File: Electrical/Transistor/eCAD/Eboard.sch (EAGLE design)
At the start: 22 parts

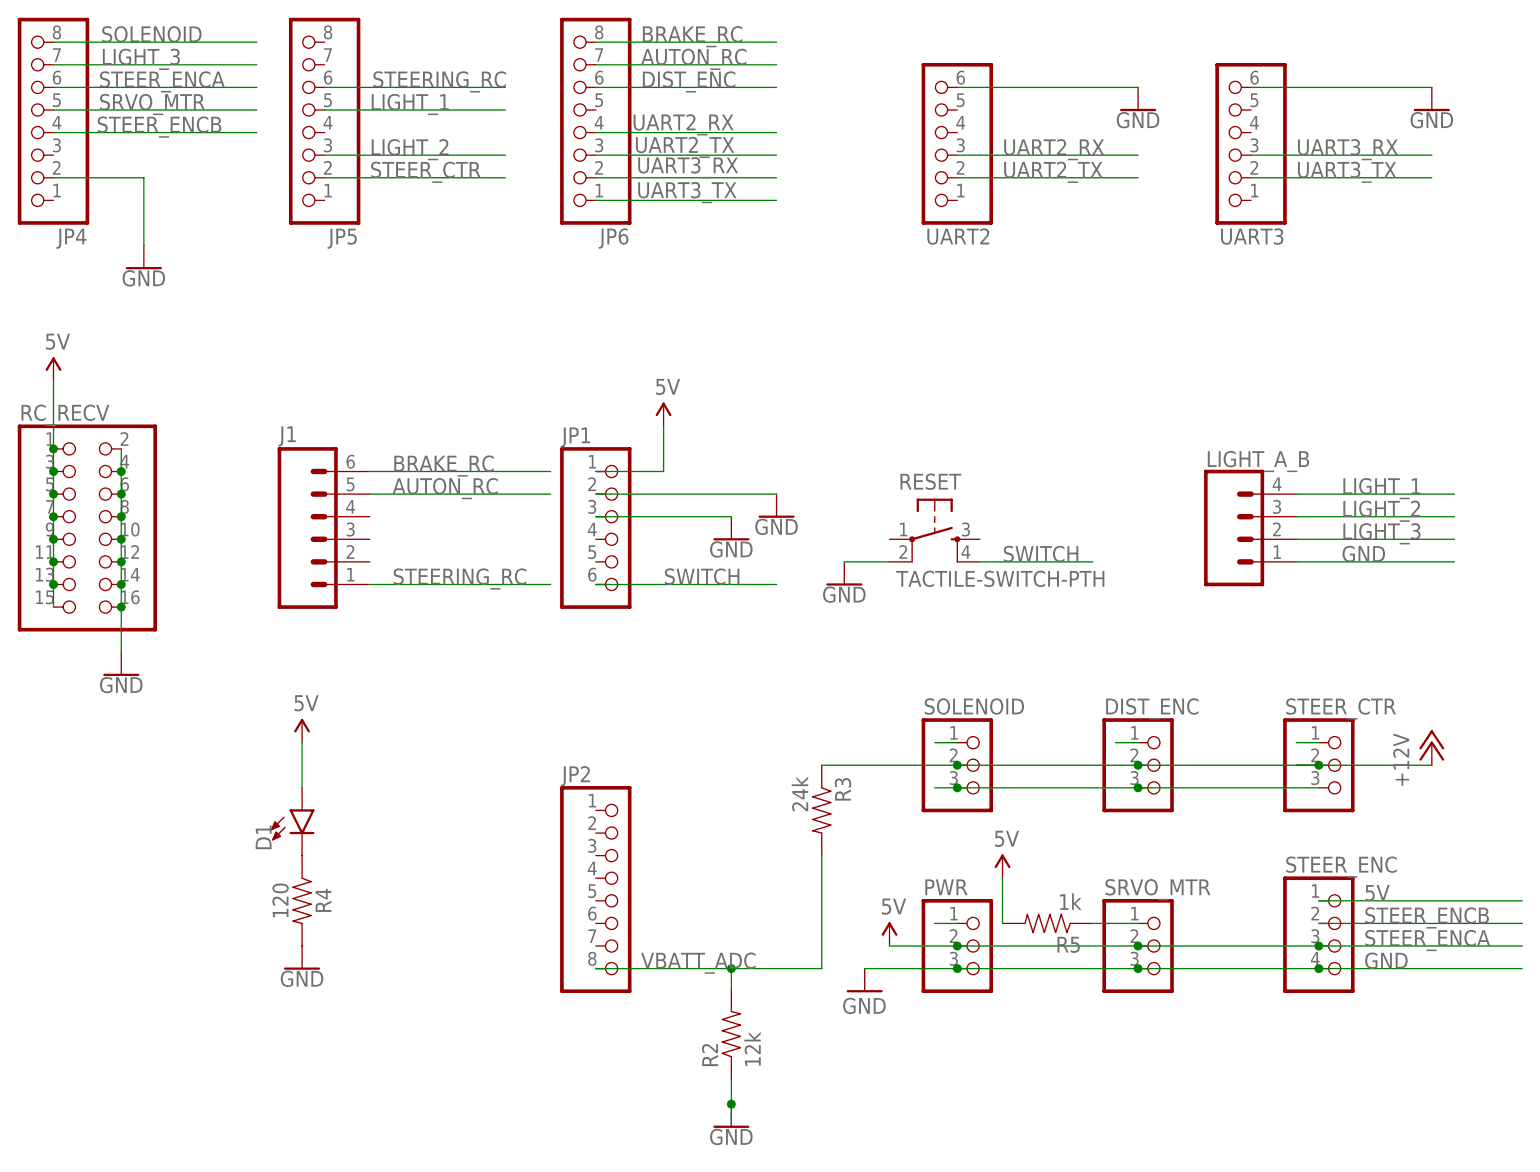
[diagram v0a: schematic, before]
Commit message: checked to see if trace connections in schematic were sensical, added ground and 5V symbols to schematic for readability, checked alignment of pin sets in board file for alignment, rerouted board file based on amendments in schematic, checked that 12V traces were 40 mils, 5V traces were 16 mils, and all other traces (incl. VBATT_ADC) were 10 mils
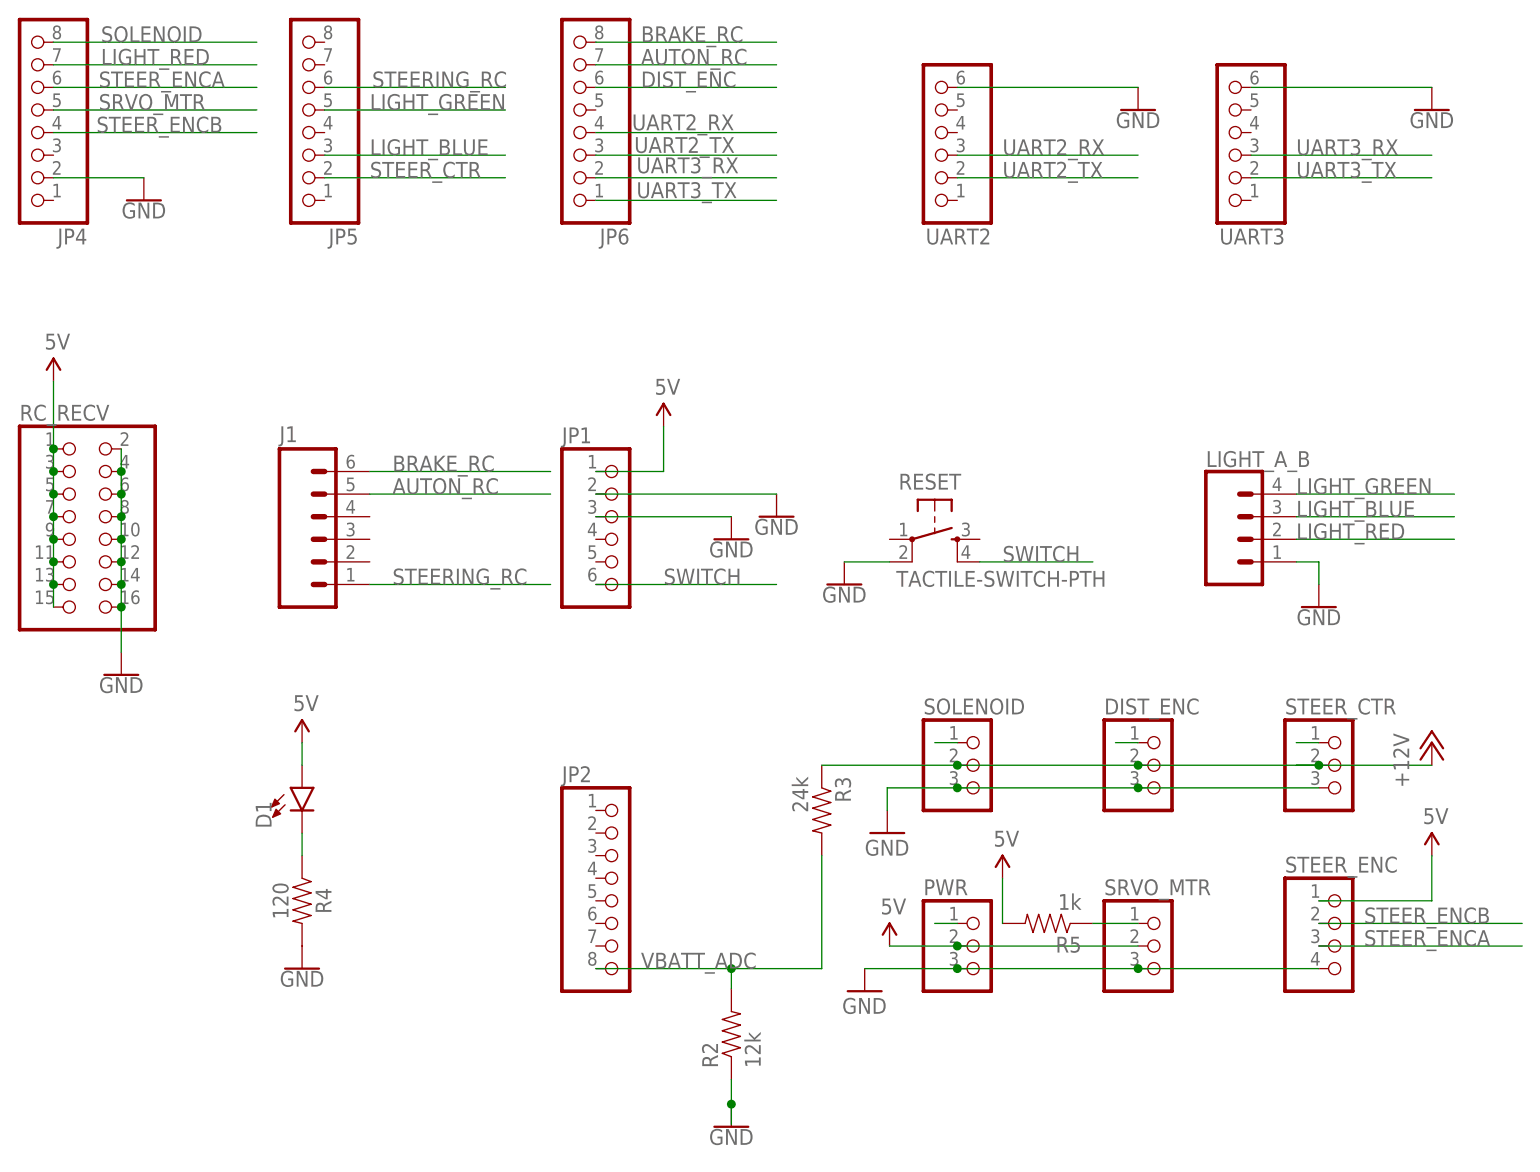
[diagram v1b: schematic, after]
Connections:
- net LIGHT_1 renamed LIGHT_GREEN
- net LIGHT_2 renamed LIGHT_BLUE
- net LIGHT_3 renamed LIGHT_RED
- net 5V: now also PWR.2, SRVO_MTR.2
- net STEER_ENCA: no longer PWR.2, SRVO_MTR.2
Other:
- moved on the sheet: D1
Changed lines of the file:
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@@
 </classes>
 <parts>
-<part name="GND2" library="supply1" deviceset="GND" device=""/>
+<part name="GND" library="supply1" deviceset="GND" device=""/>
 <part name="FRAME1" library="frames" deviceset="LETTER_L" device=""/>
 <part name="SOLENOID" library="pinhead" deviceset="PINHD-1X3" device=""/>
@@
 <part name="SUPPLY5" library="SparkFun-Aesthetics" deviceset="5V" device=""/>
 <part name="GND10" library="SparkFun-PowerSymbols" library_urn="urn:adsk.eagle:library:530" deviceset="GND" device=""/>
+<part name="GND2" library="SparkFun-PowerSymbols" library_urn="urn:adsk.eagle:library:530" deviceset="GND" device=""/>
+<part name="GND11" library="supply1" deviceset="GND" device=""/>
+<part name="SUPPLY6" library="SparkFun-Aesthetics" deviceset="5V" device=""/>
 </parts>
 <sheets>
@@
 </plain>
 <instances>
-<instance part="GND2" gate="1" x="149.606" y="71.12"/>
+<instance part="GND" gate="1" x="149.606" y="71.12"/>
 <instance part="FRAME1" gate="G$1" x="0" y="0"/>
 <instance part="FRAME1" gate="G$2" x="147.32" y="0"/>
@@
 <instance part="JP6" gate="A" x="116.84" y="170.18" rot="R180"/>
 <instance part="STEER_ENC" gate="A" x="203.2" y="76.2"/>
-<instance part="D1" gate="G$1" x="86.36" y="91.44"/>
+<instance part="D1" gate="G$1" x="86.36" y="93.98"/>
 <instance part="LIGHT_A_B" gate="G$1" x="193.04" y="121.92"/>
 <instance part="R4" gate="G$1" x="86.36" y="81.28" rot="R270"/>
@@
 <instance part="SUPPLY4" gate="G$1" x="58.42" y="139.7"/>
 <instance part="SUPPLY5" gate="G$1" x="127" y="134.62"/>
-<instance part="GND10" gate="1" x="68.58" y="152.4"/>
+<instance part="GND10" gate="1" x="68.58" y="160.02"/>
+<instance part="GND2" gate="1" x="200.66" y="114.3"/>
+<instance part="GND11" gate="1" x="152.146" y="88.9"/>
+<instance part="SUPPLY6" gate="G$1" x="213.36" y="86.36"/>
 </instances>
 <busses>
@@
 <pinref part="D1" gate="G$1" pin="A"/>
 <pinref part="SUPPLY3" gate="G$1" pin="5V"/>
-<wire x1="86.36" y1="93.98" x2="86.36" y2="99.06" width="0.1524" layer="91"/>
+<wire x1="86.36" y1="96.52" x2="86.36" y2="99.06" width="0.1524" layer="91"/>
 </segment>
 <segment>
@@
 </segment>
 <segment>
+<pinref part="PWR" gate="A" pin="2"/>
+<pinref part="SRVO_MTR" gate="A" pin="2"/>
+<wire x1="160.02" y1="76.2" x2="180.34" y2="76.2" width="0.1524" layer="91"/>
+<pinref part="SUPPLY1" gate="G$1" pin="5V"/>
+<wire x1="152.4" y1="76.2" x2="160.02" y2="76.2" width="0.1524" layer="91"/>
+<junction x="160.02" y="76.2"/>
+</segment>
+<segment>
 <pinref part="STEER_ENC" gate="A" pin="1"/>
-<label x="205.74" y="81.28" size="1.778" layer="95"/>
-<wire x1="200.66" y1="81.28" x2="223.52" y2="81.28" width="0.1524" layer="91"/>
+<wire x1="200.66" y1="81.28" x2="213.36" y2="81.28" width="0.1524" layer="91"/>
+<wire x1="213.36" y1="81.28" x2="213.36" y2="86.36" width="0.1524" layer="91"/>
+<pinref part="SUPPLY6" gate="G$1" pin="5V"/>
 </segment>
 </net>
@@
 </segment>
 <segment>
-<pinref part="GND2" gate="1" pin="GND"/>
-<wire x1="149.606" y1="73.66" x2="154.94" y2="73.66" width="0.1524" layer="91"/>
+<pinref part="GND" gate="1" pin="GND"/>
+<wire x1="149.606" y1="73.66" x2="160.02" y2="73.66" width="0.1524" layer="91"/>
 <pinref part="PWR" gate="A" pin="3"/>
-<wire x1="154.94" y1="73.66" x2="155.702" y2="73.66" width="0.1524" layer="91"/>
-<wire x1="160.02" y1="73.66" x2="155.702" y2="73.66" width="0.1524" layer="91"/>
 <pinref part="SRVO_MTR" gate="A" pin="3"/>
 <wire x1="160.02" y1="73.66" x2="180.34" y2="73.66" width="0.1524" layer="91"/>
@@
 <junction x="180.34" y="73.66"/>
 <pinref part="STEER_ENC" gate="A" pin="4"/>
-<label x="205.74" y="73.66" size="1.778" layer="95"/>
-<wire x1="200.66" y1="73.66" x2="223.52" y2="73.66" width="0.1524" layer="91"/>
-<junction x="200.66" y="73.66"/>
 <wire x1="180.34" y1="73.66" x2="200.66" y2="73.66" width="0.1524" layer="91"/>
 </segment>
@@
 <segment>
 <pinref part="SOLENOID" gate="A" pin="3"/>
-<wire x1="160.02" y1="93.98" x2="157.48" y2="93.98" width="0.1524" layer="91"/>
-<junction x="160.02" y="93.98"/>
 <pinref part="DIST_ENC" gate="A" pin="3"/>
 <junction x="180.34" y="93.98"/>
@@
 <wire x1="180.34" y1="93.98" x2="200.66" y2="93.98" width="0.1524" layer="91"/>
 <wire x1="160.02" y1="93.98" x2="180.34" y2="93.98" width="0.1524" layer="91"/>
-</segment>
-<segment>
-<pinref part="LIGHT_A_B" gate="G$1" pin="1"/>
-<label x="203.2" y="119.38" size="1.778" layer="95"/>
-<wire x1="198.12" y1="119.38" x2="215.9" y2="119.38" width="0.1524" layer="91"/>
+<pinref part="GND11" gate="1" pin="GND"/>
+<wire x1="160.02" y1="93.98" x2="152.146" y2="93.98" width="0.1524" layer="91"/>
+<wire x1="152.146" y1="93.98" x2="152.146" y2="91.44" width="0.1524" layer="91"/>
+<junction x="160.02" y="93.98"/>
 </segment>
 <segment>
@@
 <pinref part="JP4" gate="A" pin="2"/>
 <wire x1="58.42" y1="162.56" x2="68.58" y2="162.56" width="0.1524" layer="91"/>
-<wire x1="68.58" y1="162.56" x2="68.58" y2="154.94" width="0.1524" layer="91"/>
 <pinref part="GND10" gate="1" pin="GND"/>
 </segment>
@@
 <pinref part="R4" gate="G$1" pin="2"/>
 <pinref part="GND4" gate="1" pin="GND"/>
+</segment>
+<segment>
+<pinref part="LIGHT_A_B" gate="G$1" pin="1"/>
+<pinref part="GND2" gate="1" pin="GND"/>
+<wire x1="198.12" y1="119.38" x2="200.66" y2="119.38" width="0.1524" layer="91"/>
+<wire x1="200.66" y1="119.38" x2="200.66" y2="116.84" width="0.1524" layer="91"/>
 </segment>
 </net>
@@
 </segment>
 <segment>
-<pinref part="PWR" gate="A" pin="2"/>
-<pinref part="SRVO_MTR" gate="A" pin="2"/>
-<wire x1="160.02" y1="76.2" x2="180.34" y2="76.2" width="0.1524" layer="91"/>
-<junction x="180.34" y="76.2"/>
 <pinref part="STEER_ENC" gate="A" pin="3"/>
+<wire x1="200.66" y1="76.2" x2="223.52" y2="76.2" width="0.1524" layer="91"/>
 <label x="205.74" y="76.2" size="1.778" layer="95"/>
-<wire x1="200.66" y1="76.2" x2="223.52" y2="76.2" width="0.1524" layer="91"/>
-<junction x="200.66" y="76.2"/>
-<wire x1="180.34" y1="76.2" x2="200.66" y2="76.2" width="0.1524" layer="91"/>
-<pinref part="SUPPLY1" gate="G$1" pin="5V"/>
-<wire x1="152.4" y1="76.2" x2="160.02" y2="76.2" width="0.1524" layer="91"/>
-<junction x="160.02" y="76.2"/>
 </segment>
 </net>
@@
 </segment>
 </net>
-<net name="LIGHT_1" class="0">
+<net name="LIGHT_GREEN" class="0">
 <segment>
 <pinref part="LIGHT_A_B" gate="G$1" pin="4"/>
-<label x="203.2" y="127" size="1.778" layer="95"/>
+<label x="198.12" y="127" size="1.778" layer="95"/>
 <wire x1="198.12" y1="127" x2="215.9" y2="127" width="0.1524" layer="91"/>
 </segment>
@@
 </segment>
 </net>
-<net name="LIGHT_2" class="0">
+<net name="LIGHT_BLUE" class="0">
 <segment>
 <pinref part="LIGHT_A_B" gate="G$1" pin="3"/>
-<label x="203.2" y="124.46" size="1.778" layer="95"/>
+<label x="198.12" y="124.46" size="1.778" layer="95"/>
 <wire x1="198.12" y1="124.46" x2="215.9" y2="124.46" width="0.1524" layer="91"/>
 </segment>
@@
 </segment>
 </net>
-<net name="LIGHT_3" class="0">
+<net name="LIGHT_RED" class="0">
 <segment>
 <pinref part="LIGHT_A_B" gate="G$1" pin="2"/>
-<label x="203.2" y="121.92" size="1.778" layer="95"/>
+<label x="198.12" y="121.92" size="1.778" layer="95"/>
 <wire x1="198.12" y1="121.92" x2="215.9" y2="121.92" width="0.1524" layer="91"/>
 </segment>
@@
 <pinref part="D1" gate="G$1" pin="C"/>
 <pinref part="R4" gate="G$1" pin="1"/>
-</segment>
-</net>
+<wire x1="86.36" y1="88.9" x2="86.36" y2="86.36" width="0.1524" layer="91"/>
+</segment>
+</net>

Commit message: updated the light names, updated the offset on shield to match arduino mega to resolve alignment issues in 1.7, updated silkscreen with labels for pins, added dimensions to tDocu layer in inches, double checked pins match on shield, checked that orientations for all pins were correct on board
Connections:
- net 5V: no longer JP1.1
- net LIGHT_BLUE: now also JP5.5, LIGHT_A_B.4; no longer JP5.3, LIGHT_A_B.3
- net LIGHT_GREEN: now also JP5.3, LIGHT_A_B.3; no longer JP5.5, LIGHT_A_B.4
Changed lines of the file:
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@@
 <part name="SUPPLY3" library="SparkFun-Aesthetics" deviceset="5V" device=""/>
 <part name="SUPPLY4" library="SparkFun-Aesthetics" deviceset="5V" device=""/>
-<part name="SUPPLY5" library="SparkFun-Aesthetics" deviceset="5V" device=""/>
 <part name="GND10" library="SparkFun-PowerSymbols" library_urn="urn:adsk.eagle:library:530" deviceset="GND" device=""/>
 <part name="GND2" library="SparkFun-PowerSymbols" library_urn="urn:adsk.eagle:library:530" deviceset="GND" device=""/>
@@
 <instance part="SUPPLY3" gate="G$1" x="86.36" y="99.06"/>
 <instance part="SUPPLY4" gate="G$1" x="58.42" y="139.7"/>
-<instance part="SUPPLY5" gate="G$1" x="127" y="134.62"/>
 <instance part="GND10" gate="1" x="68.58" y="160.02"/>
 <instance part="GND2" gate="1" x="200.66" y="114.3"/>
@@
 </segment>
 <segment>
-<pinref part="JP1" gate="A" pin="1"/>
-<wire x1="119.38" y1="129.54" x2="127" y2="129.54" width="0.1524" layer="91"/>
-<wire x1="127" y1="129.54" x2="127" y2="134.62" width="0.1524" layer="91"/>
-<pinref part="SUPPLY5" gate="G$1" pin="5V"/>
-</segment>
-<segment>
 <pinref part="PWR" gate="A" pin="2"/>
 <pinref part="SRVO_MTR" gate="A" pin="2"/>
@@
 <net name="LIGHT_GREEN" class="0">
 <segment>
+<pinref part="JP5" gate="A" pin="3"/>
+<label x="93.98" y="165.1" size="1.778" layer="95"/>
+<wire x1="88.9" y1="165.1" x2="109.22" y2="165.1" width="0.1524" layer="91"/>
+</segment>
+<segment>
+<pinref part="LIGHT_A_B" gate="G$1" pin="3"/>
+<label x="198.12" y="124.46" size="1.778" layer="95"/>
+<wire x1="198.12" y1="124.46" x2="215.9" y2="124.46" width="0.1524" layer="91"/>
+</segment>
+</net>
+<net name="LIGHT_BLUE" class="0">
+<segment>
+<pinref part="JP5" gate="A" pin="5"/>
+<label x="93.98" y="170.18" size="1.778" layer="95"/>
+<wire x1="88.9" y1="170.18" x2="109.22" y2="170.18" width="0.1524" layer="91"/>
+</segment>
+<segment>
 <pinref part="LIGHT_A_B" gate="G$1" pin="4"/>
 <label x="198.12" y="127" size="1.778" layer="95"/>
 <wire x1="198.12" y1="127" x2="215.9" y2="127" width="0.1524" layer="91"/>
 </segment>
-<segment>
-<pinref part="JP5" gate="A" pin="5"/>
-<label x="93.98" y="170.18" size="1.778" layer="95"/>
-<wire x1="88.9" y1="170.18" x2="109.22" y2="170.18" width="0.1524" layer="91"/>
-</segment>
-</net>
-<net name="LIGHT_BLUE" class="0">
-<segment>
-<pinref part="LIGHT_A_B" gate="G$1" pin="3"/>
-<label x="198.12" y="124.46" size="1.778" layer="95"/>
-<wire x1="198.12" y1="124.46" x2="215.9" y2="124.46" width="0.1524" layer="91"/>
-</segment>
-<segment>
-<pinref part="JP5" gate="A" pin="3"/>
-<label x="93.98" y="165.1" size="1.778" layer="95"/>
-<wire x1="88.9" y1="165.1" x2="109.22" y2="165.1" width="0.1524" layer="91"/>
-</segment>
-</net>
+</net>

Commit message: added 12V silkscreen, changed servo mtr to two-pin connector, rerouted accordingly
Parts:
- removed SRVO_MTR: (no value), pinhead:PINHD-1X3
- added SERVO_MTR: (no value), SparkFun-Connectors:CONN_02
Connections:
- new net N$3: STEER_ENC.4
- net 5V: no longer SRVO_MTR.2
- net GND: now also SERVO_MTR.2; no longer SRVO_MTR.3, STEER_ENC.4
- net SRVO_MTR: now also SERVO_MTR.1; no longer SRVO_MTR.1
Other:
- moved on the sheet: R5
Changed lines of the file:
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@@
 <part name="DIST_ENC" library="pinhead" deviceset="PINHD-1X3" device=""/>
 <part name="STEER_CTR" library="pinhead" deviceset="PINHD-1X3" device=""/>
-<part name="SRVO_MTR" library="pinhead" deviceset="PINHD-1X3" device=""/>
 <part name="RC_RECV" library="pinhead" deviceset="PINHD-2X8" device=""/>
 <part name="SUPPLY1" library="SparkFun-Aesthetics" deviceset="5V" device=""/>
@@
 <part name="GND11" library="supply1" deviceset="GND" device=""/>
 <part name="SUPPLY6" library="SparkFun-Aesthetics" deviceset="5V" device=""/>
+<part name="SERVO_MTR" library="SparkFun-Connectors" library_urn="urn:adsk.eagle:library:513" deviceset="CONN_02" device="" package3d_urn="urn:adsk.eagle:package:38039/1"/>
 </parts>
 <sheets>
@@
 <instance part="DIST_ENC" gate="A" x="182.88" y="96.52"/>
 <instance part="STEER_CTR" gate="A" x="203.2" y="96.52"/>
-<instance part="SRVO_MTR" gate="A" x="182.88" y="76.2"/>
 <instance part="RC_RECV" gate="A" x="60.96" y="124.46"/>
 <instance part="SUPPLY1" gate="G$1" x="152.4" y="76.2"/>
@@
 <instance part="GND4" gate="1" x="86.36" y="73.66"/>
 <instance part="SUPPLY2" gate="G$1" x="165.1" y="83.82"/>
-<instance part="R5" gate="G$1" x="170.18" y="78.74" rot="R180"/>
+<instance part="R5" gate="G$1" x="170.18" y="83.82" rot="R180"/>
 <instance part="GND5" gate="1" x="180.34" y="170.18"/>
 <instance part="GND6" gate="1" x="213.36" y="170.18"/>
@@
 <instance part="GND11" gate="1" x="152.146" y="88.9"/>
 <instance part="SUPPLY6" gate="G$1" x="213.36" y="86.36"/>
+<instance part="SERVO_MTR" gate="G$1" x="182.88" y="76.2" rot="R180"/>
 </instances>
 <busses>
@@
 <pinref part="R5" gate="G$1" pin="2"/>
 <pinref part="SUPPLY2" gate="G$1" pin="5V"/>
-<wire x1="165.1" y1="78.74" x2="165.1" y2="83.82" width="0.1524" layer="91"/>
 </segment>
 <segment>
@@
 <segment>
 <pinref part="PWR" gate="A" pin="2"/>
-<pinref part="SRVO_MTR" gate="A" pin="2"/>
-<wire x1="160.02" y1="76.2" x2="180.34" y2="76.2" width="0.1524" layer="91"/>
 <pinref part="SUPPLY1" gate="G$1" pin="5V"/>
 <wire x1="152.4" y1="76.2" x2="160.02" y2="76.2" width="0.1524" layer="91"/>
-<junction x="160.02" y="76.2"/>
 </segment>
 <segment>
@@
 </segment>
 <segment>
+<pinref part="PWR" gate="A" pin="3"/>
 <pinref part="GND" gate="1" pin="GND"/>
 <wire x1="149.606" y1="73.66" x2="160.02" y2="73.66" width="0.1524" layer="91"/>
-<pinref part="PWR" gate="A" pin="3"/>
-<pinref part="SRVO_MTR" gate="A" pin="3"/>
-<wire x1="160.02" y1="73.66" x2="180.34" y2="73.66" width="0.1524" layer="91"/>
+<pinref part="SERVO_MTR" gate="G$1" pin="2"/>
+<wire x1="160.02" y1="73.66" x2="175.26" y2="73.66" width="0.1524" layer="91"/>
 <junction x="160.02" y="73.66"/>
-<junction x="180.34" y="73.66"/>
-<pinref part="STEER_ENC" gate="A" pin="4"/>
-<wire x1="180.34" y1="73.66" x2="200.66" y2="73.66" width="0.1524" layer="91"/>
 </segment>
 <segment>
@@
 </segment>
 <segment>
-<pinref part="SRVO_MTR" gate="A" pin="1"/>
-<wire x1="180.34" y1="78.74" x2="175.26" y2="78.74" width="0.1524" layer="91"/>
 <pinref part="R5" gate="G$1" pin="1"/>
+<pinref part="SERVO_MTR" gate="G$1" pin="1"/>
+<wire x1="175.26" y1="83.82" x2="175.26" y2="76.2" width="0.1524" layer="91"/>
 </segment>
 </net>
@@
 </segment>
 </net>
+<net name="N$3" class="0">
+<segment>
+<pinref part="STEER_ENC" gate="A" pin="4"/>
+<wire x1="195.58" y1="73.66" x2="200.66" y2="73.66" width="0.1524" layer="91"/>
+</segment>
+</net>
